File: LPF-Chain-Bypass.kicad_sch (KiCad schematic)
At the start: 2 parts, among them K1 HK19F-DCxxV-SHC, K2 HK19F-DCxxV-SHC

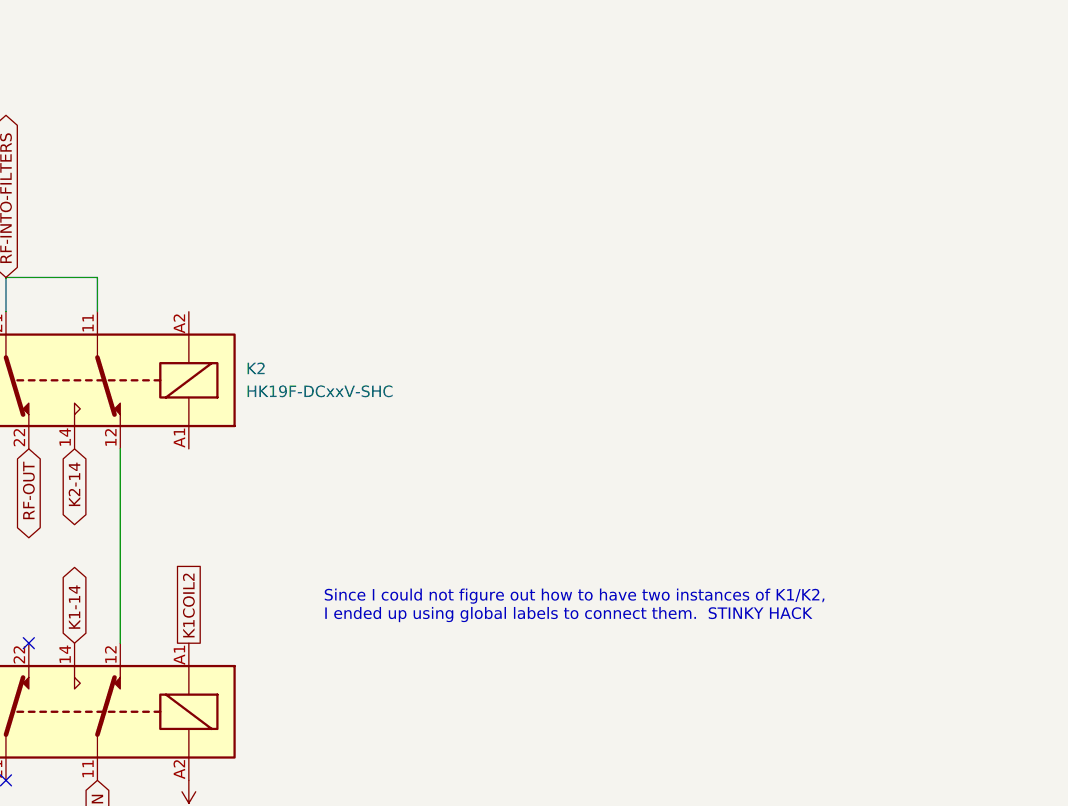
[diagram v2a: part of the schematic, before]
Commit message: got rid of K11 which was alias for K2.  Figured out RELAY-SYNC as a way of making sure K1 & K2 operate in sync
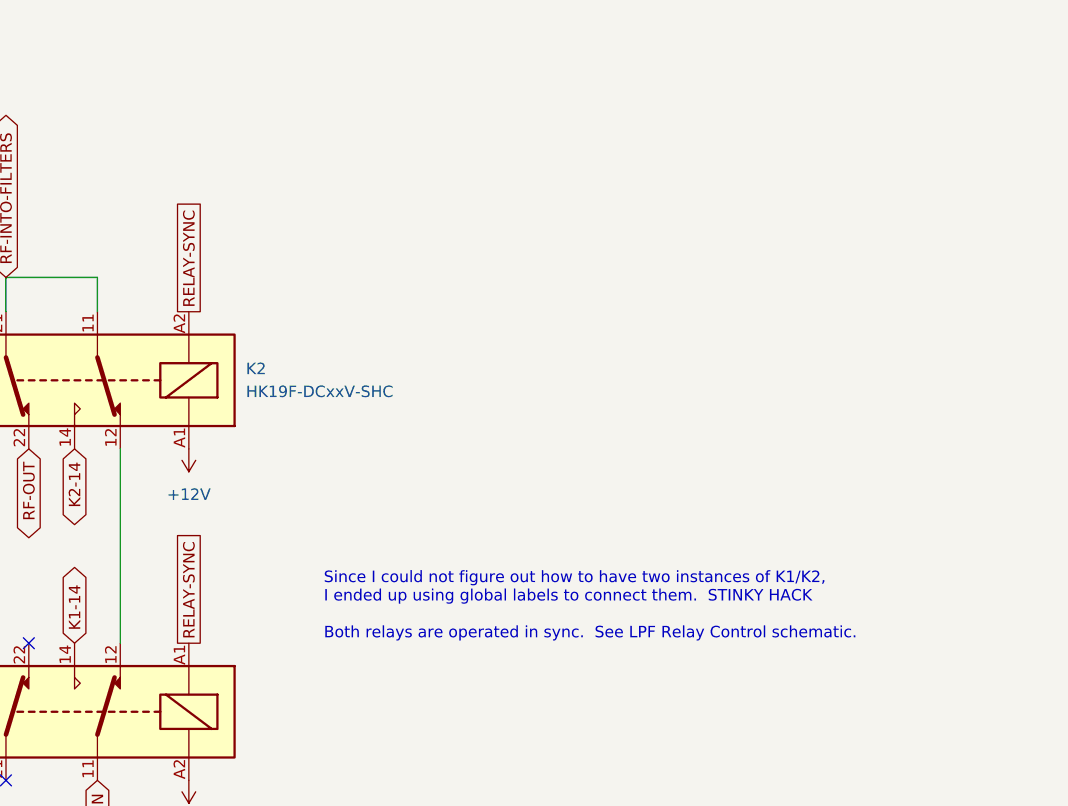
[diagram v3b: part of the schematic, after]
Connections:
- net K1COIL2 is gone; now on net RELAY-SYNC: K1.A1
- net +12V: now also K2.A1
- net RELAY-SYNC: now reaches K2.A2
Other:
- note added: "Since I could not figure out how to have two instances of K1/K2, I ended up using global labels to connect them. STINKY HACK Both relays are operated in sync. See LPF Relay Control schematic."
- note removed: "Since I could not figure out how to have two instances of K1/K2, I ended up using global labels to connect them. STINKY HACK"
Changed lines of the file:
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@@
 		)
 	)
-	(text "Since I could not figure out how to have two instances of K1/K2,\nI ended up using global labels to connect them.  STINKY HACK"
+	(text "Since I could not figure out how to have two instances of K1/K2,\nI ended up using global labels to connect them.  STINKY HACK\n\nBoth relays are operated in sync.  See LPF Relay Control schematic."
 		(exclude_from_sim no)
 		(at 166.116 96.266 0)
@@
 		)
 	)
+	(global_label "RELAY-SYNC"
+		(shape passive)
+		(at 151.13 63.5 90)
+		(fields_autoplaced yes)
+		(effects
+			(font
+				(size 1.27 1.27)
+			)
+			(justify left)
+		)
+		(property "Intersheetrefs" "${INTERSHEET_REFS}"
+			(at 151.13 49.3404 90)
+			(effects
+				(font
+					(size 1.27 1.27)
+				)
+				(justify left)
+				(hide yes)
+			)
+		)
+	)
 	(global_label "RF-INTO-FILTERS"
 		(shape bidirectional)
@@
 		)
 	)
-	(global_label "K1COIL2"
+	(global_label "RELAY-SYNC"
 		(shape passive)
 		(at 151.13 100.33 90)
@@
 		)
 		(property "Intersheetrefs" "${INTERSHEET_REFS}"
-			(at 151.13 90.3433 90)
+			(at 151.13 86.1704 90)
 			(effects
 				(font
@@
 					(unit 1)
 				)
+			)
+		)
+	)
+	(symbol
+		(lib_id "power:+12V")
+		(at 151.13 78.74 180)
+		(unit 1)
+		(exclude_from_sim no)
+		(in_bom yes)
+		(on_board yes)
+		(dnp no)
+		(fields_autoplaced yes)
+		(property "Reference" "#PWR042"
+			(at 151.13 74.93 0)
+			(effects
+				(font
+					(size 1.27 1.27)
+				)
+				(hide yes)
+			)
+		)
+		(property "Value" "+12V"
+			(at 151.13 83.82 0)
+			(effects
+				(font
+					(size 1.27 1.27)
+				)
+			)
+		)
+		(property "Footprint" ""
+			(at 151.13 78.74 0)
+			(effects
+				(font
+					(size 1.27 1.27)
+				)
+				(hide yes)
+			)
+		)
+		(property "Datasheet" ""
+			(at 151.13 78.74 0)
+			(effects
+				(font
+					(size 1.27 1.27)
+				)
+				(hide yes)
+			)
+		)
+		(property "Description" "Power symbol creates a global label with name \"+12V\""
+			(at 151.13 78.74 0)
+			(effects
+				(font
+					(size 1.27 1.27)
+				)
+				(hide yes)
+			)
+		)
+		(pin "1"
+		)
+		(instances
+			(project "QMX-amp"
+				(path "/e63e39d7-6ac0-4ffd-8aa3-1841a4541b55/437da5b9-3c1b-43a3-b733-5d9a574d228b"
+					(reference "#PWR042")
+					(unit 1)
+				)
